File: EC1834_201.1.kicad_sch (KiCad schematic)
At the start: 91 parts, among them X6 RESET_BTN

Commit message: Small improvements
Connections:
- net TDYTODMA is gone; now on net RDYTODMA: D50.6 (RDY)
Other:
- note added: "H PullUp R10"
- note added: "H, wenn kein Speicherzugriff"
- note added: "L in CPU Zyklus T3 oder RDY LOW"
- note added: "L, wenn kein Speicherzugriff"
- note added: "offen!"
- note added: "←"

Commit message: Fixed wrong symbol (some DL008 are 74S00)
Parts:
- D10, D32, D39: value DL000D -> 74S00
- D16: value DL000D -> DL000
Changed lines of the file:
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@@
     (in_bom yes) (on_board yes)
     (property "Reference" "D32" (id 0) (at 372.11 125.73 0))
-    (property "Value" "DL000D" (id 1) (at 372.11 119.7864 0))
+    (property "Value" "74S00" (id 1) (at 372.11 119.7864 0))
     (property "Footprint" "Package_DIP:DIP-14_W7.62mm" (id 2) (at 372.11 125.73 0)
       (effects (font (size 1.27 1.27)) hide)
@@
     (in_bom yes) (on_board yes)
     (property "Reference" "D39" (id 0) (at 302.26 92.71 0))
-    (property "Value" "DL000D" (id 1) (at 302.26 86.7664 0))
+    (property "Value" "74S00" (id 1) (at 302.26 86.7664 0))
     (property "Footprint" "Package_DIP:DIP-14_W7.62mm" (id 2) (at 302.26 92.71 0)
       (effects (font (size 1.27 1.27)) hide)
@@
     (in_bom yes) (on_board yes)
     (property "Reference" "D39" (id 0) (at 290.83 90.17 0))
-    (property "Value" "DL000D" (id 1) (at 290.83 84.2264 0))
+    (property "Value" "74S00" (id 1) (at 290.83 84.2264 0))
     (property "Footprint" "Package_DIP:DIP-14_W7.62mm" (id 2) (at 290.83 90.17 0)
       (effects (font (size 1.27 1.27)) hide)
@@
     (in_bom yes) (on_board yes)
     (property "Reference" "D10" (id 0) (at 102.87 154.94 0))
-    (property "Value" "DL000D" (id 1) (at 102.87 146.6596 0))
+    (property "Value" "74S00" (id 1) (at 102.87 146.6596 0))
     (property "Footprint" "Package_DIP:DIP-14_W7.62mm" (id 2) (at 102.87 152.4 0)
       (effects (font (size 1.27 1.27)) hide)
@@
     (in_bom yes) (on_board yes)
     (property "Reference" "D39" (id 0) (at 204.47 187.96 0))
-    (property "Value" "DL000D" (id 1) (at 204.47 182.0164 0))
+    (property "Value" "74S00" (id 1) (at 204.47 182.0164 0))
     (property "Footprint" "Package_DIP:DIP-14_W7.62mm" (id 2) (at 204.47 187.96 0)
       (effects (font (size 1.27 1.27)) hide)
@@
     (in_bom yes) (on_board yes)
     (property "Reference" "D32" (id 0) (at 102.87 88.9 0))
-    (property "Value" "DL000D" (id 1) (at 102.87 81.8896 0))
+    (property "Value" "74S00" (id 1) (at 102.87 81.8896 0))
     (property "Footprint" "Package_DIP:DIP-14_W7.62mm" (id 2) (at 102.87 87.63 0)
       (effects (font (size 1.27 1.27)) hide)
@@
     (in_bom yes) (on_board yes)
     (property "Reference" "D16" (id 0) (at 102.87 43.18 0))
-    (property "Value" "DL000D" (id 1) (at 102.87 34.8996 0))
+    (property "Value" "DL000" (id 1) (at 102.87 34.8996 0))
     (property "Footprint" "Package_DIP:DIP-14_W7.62mm" (id 2) (at 102.87 40.64 0)
       (effects (font (size 1.27 1.27)) hide)
@@
     (in_bom yes) (on_board yes)
     (property "Reference" "D16" (id 0) (at 151.13 43.18 0))
-    (property "Value" "DL000D" (id 1) (at 151.13 37.2364 0))
+    (property "Value" "DL000" (id 1) (at 151.13 37.2364 0))
     (property "Footprint" "Package_DIP:DIP-14_W7.62mm" (id 2) (at 151.13 43.18 0)
       (effects (font (size 1.27 1.27)) hide)
@@
     (in_bom yes) (on_board yes)
     (property "Reference" "D32" (id 0) (at 129.54 54.61 0))
-    (property "Value" "DL000D" (id 1) (at 129.54 48.6664 0))
+    (property "Value" "74S00" (id 1) (at 129.54 48.6664 0))
     (property "Footprint" "Package_DIP:DIP-14_W7.62mm" (id 2) (at 129.54 54.61 0)
       (effects (font (size 1.27 1.27)) hide)
@@
     (in_bom yes) (on_board yes)
     (property "Reference" "D32" (id 0) (at 151.13 58.42 0))
-    (property "Value" "DL000D" (id 1) (at 151.13 51.4096 0))
+    (property "Value" "74S00" (id 1) (at 151.13 51.4096 0))
     (property "Footprint" "Package_DIP:DIP-14_W7.62mm" (id 2) (at 151.13 57.15 0)
       (effects (font (size 1.27 1.27)) hide)

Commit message: Modifications to pass most ERC checks modified symbols for ERC check Added some notes
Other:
- note added: "DMA Page Register Steuerung"

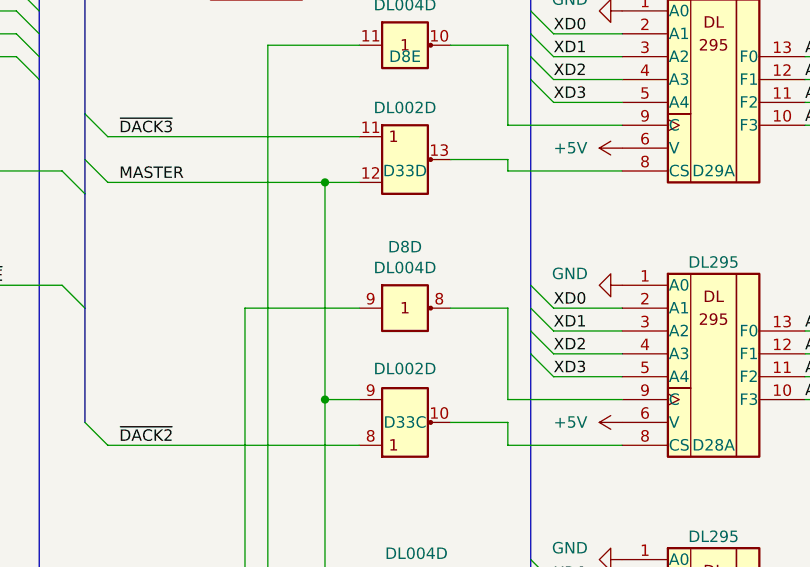
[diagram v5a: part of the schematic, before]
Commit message: Updated ec1834 symbols Fixed missing D8-D15 on bus connector Updated PDFs
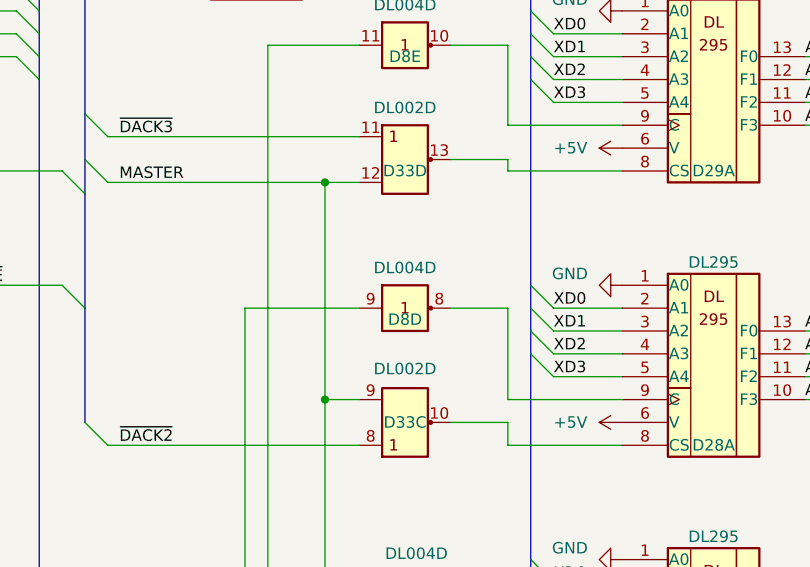
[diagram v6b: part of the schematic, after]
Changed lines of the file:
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@@
   (symbol (lib_id "RFT_Digitalschaltkreise:DL004D") (at 298.45 316.23 0) (unit 4)
     (in_bom yes) (on_board yes)
-    (property "Reference" "D8" (id 0) (at 298.45 309.4482 0))
+    (property "Reference" "D8" (id 0) (at 298.45 317.5 0))
     (property "Value" "DL004D" (id 1) (at 298.45 311.7596 0))
     (property "Footprint" "Package_DIP:DIP-14_W7.62mm" (id 2) (at 298.45 316.23 0)

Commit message: Changed WD1-5 connections - open > bridged
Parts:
- WD1, WD2, WD3: symbol Jumper:SolderJumper_2_Open -> Jumper:SolderJumper_2_Bridged
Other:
- note removed: "Durch WD2 deaktiviert"
- note removed: "Durch WD3 deaktiviert"
- note removed: "offen!"
- moved on the sheet: D11B, R12G
